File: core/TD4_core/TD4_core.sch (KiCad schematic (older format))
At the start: 7 parts, among them J1 Conn_02x32_Row_Letter_First

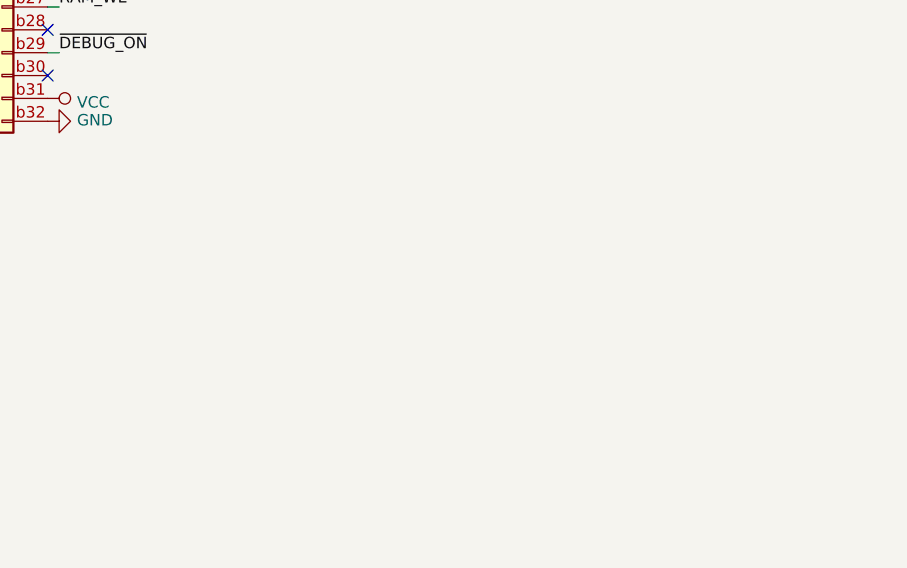
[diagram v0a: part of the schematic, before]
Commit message: Added IN bus pull-ups in core
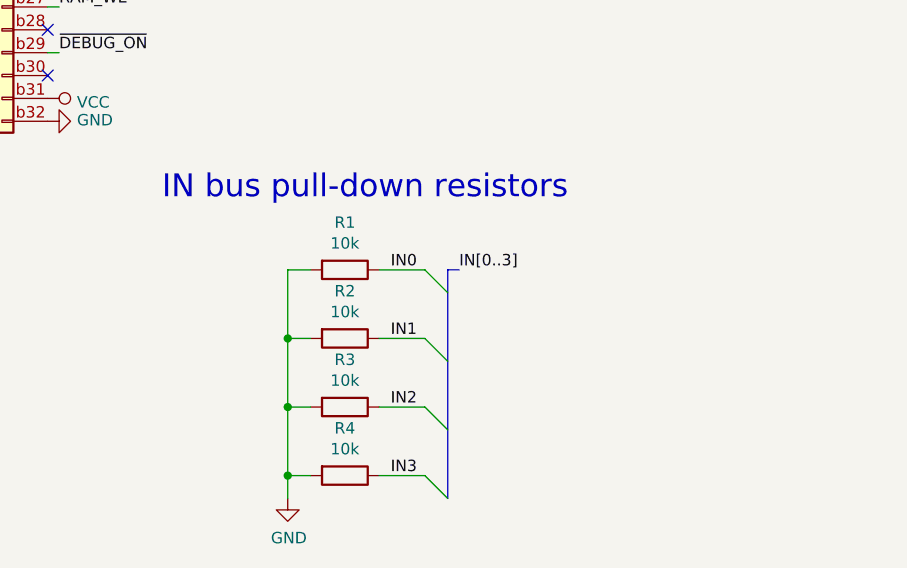
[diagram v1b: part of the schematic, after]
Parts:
- added R1, R2, R3, R4: 10k, Resistor_SMD:R_0805_2012Metric, symbol Device:R
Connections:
- net GND: now also R1.2, R2.2, R3.2, R4.2
- net IN0: now also R1.1
- net IN1: now also R2.1
- net IN2: now also R3.1
- net IN3: now also R4.1
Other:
- note added: "IN bus pull-down resistors"
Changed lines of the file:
@@
 	0    1    1    0
 $EndComp
+Entry Wire Line
+	3600 6200 3700 6300
+Entry Wire Line
+	3600 6500 3700 6600
+Wire Wire Line
+	3600 6200 3400 6200
+Text Label 3750 6200 0    50   ~ 0
+IN[0..3]
+Wire Bus Line
+	3750 6200 3700 6200
+Text Label 3450 6200 0    50   ~ 0
+IN0
+$Comp
+L Device:R R1
+U 1 1 5C6E6599
+P 3250 6200
+F 0 "R1" V 3043 6200 50  0000 C CNN
+F 1 "10k" V 3134 6200 50  0000 C CNN
+F 2 "Resistor_SMD:R_0805_2012Metric" V 3180 6200 50  0001 C CNN
+F 3 "~" H 3250 6200 50  0001 C CNN
+	1    3250 6200
+	0    1    1    0
+$EndComp
+Wire Wire Line
+	3600 6500 3400 6500
+Text Label 3450 6500 0    50   ~ 0
+IN1
+$Comp
+L Device:R R2
+U 1 1 5C6EC65C
+P 3250 6500
+F 0 "R2" V 3043 6500 50  0000 C CNN
+F 1 "10k" V 3134 6500 50  0000 C CNN
+F 2 "Resistor_SMD:R_0805_2012Metric" V 3180 6500 50  0001 C CNN
+F 3 "~" H 3250 6500 50  0001 C CNN
+	1    3250 6500
+	0    1    1    0
+$EndComp
+Entry Wire Line
+	3600 6800 3700 6900
+Entry Wire Line
+	3600 7100 3700 7200
+Wire Wire Line
+	3600 6800 3400 6800
+Text Label 3450 6800 0    50   ~ 0
+IN2
+$Comp
+L Device:R R3
+U 1 1 5C6F2817
+P 3250 6800
+F 0 "R3" V 3043 6800 50  0000 C CNN
+F 1 "10k" V 3134 6800 50  0000 C CNN
+F 2 "Resistor_SMD:R_0805_2012Metric" V 3180 6800 50  0001 C CNN
+F 3 "~" H 3250 6800 50  0001 C CNN
+	1    3250 6800
+	0    1    1    0
+$EndComp
+Wire Wire Line
+	3600 7100 3400 7100
+Text Label 3450 7100 0    50   ~ 0
+IN3
+$Comp
+L Device:R R4
+U 1 1 5C6F2820
+P 3250 7100
+F 0 "R4" V 3043 7100 50  0000 C CNN
+F 1 "10k" V 3134 7100 50  0000 C CNN
+F 2 "Resistor_SMD:R_0805_2012Metric" V 3180 7100 50  0001 C CNN
+F 3 "~" H 3250 7100 50  0001 C CNN
+	1    3250 7100
+	0    1    1    0
+$EndComp
+Wire Wire Line
+	3100 7100 3000 7100
+Wire Wire Line
+	3000 7100 3000 6800
+Wire Wire Line
+	3000 6200 3100 6200
+Wire Wire Line
+	3100 6500 3000 6500
+Connection ~ 3000 6500
+Wire Wire Line
+	3000 6500 3000 6200
+Wire Wire Line
+	3000 6800 3100 6800
+Connection ~ 3000 6800
+Wire Wire Line
+	3000 6800 3000 6500
+Text Notes 2450 5900 0    100  ~ 0
+IN bus pull-down resistors
+Wire Wire Line
+	3000 7100 3000 7200
 Wire Bus Line
 	4450 2600 4450 2900
@@
 	4450 4400 4450 4700
 Wire Bus Line
-	1050 3750 1050 4150
+	3700 6200 3700 7200
+Wire Bus Line
+	3750 4150 3750 4500
+Wire Bus Line
+	3750 3250 3750 3600
+Wire Bus Line
+	2350 4550 2350 4950
+Wire Bus Line
+	4450 3400 4450 3800
+Wire Bus Line
+	3750 2350 3750 2700
 Wire Bus Line
 	2350 3750 2350 4150
 Wire Bus Line
-	3750 2350 3750 2700
+	1050 3750 1050 4150
 Wire Bus Line
-	4450 3400 4450 3800
-Wire Bus Line
-	2350 4550 2350 4950
-Wire Bus Line
-	3750 3250 3750 3600
-Wire Bus Line
-	3750 4150 3750 4500
-Wire Bus Line
-	1050 4550 1050 5350
+	2350 2850 2350 3650
 Wire Bus Line
 	1050 2850 1050 3650
 Wire Bus Line
-	2350 2850 2350 3650
+	1050 4550 1050 5350
+Connection ~ 3000 7100
+$Comp
+L power:GND #PWR0149
+U 1 1 5C728A8A
+P 3000 7200
+F 0 "#PWR0149" H 3000 6950 50  0001 C CNN
+F 1 "GND" H 3005 7027 50  0000 C CNN
+F 2 "" H 3000 7200 50  0001 C CNN
+F 3 "" H 3000 7200 50  0001 C CNN
+	1    3000 7200
+	1    0    0    -1
+$EndComp
 $EndSCHEMATC
